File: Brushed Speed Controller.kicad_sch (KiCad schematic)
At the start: 18 parts, among them J1 Input, J2 Output, U1 TC4427, U2 TC4427, U3 SQJ500AEP-T1_GE3, U5 SQJ500AEP-T1_GE3

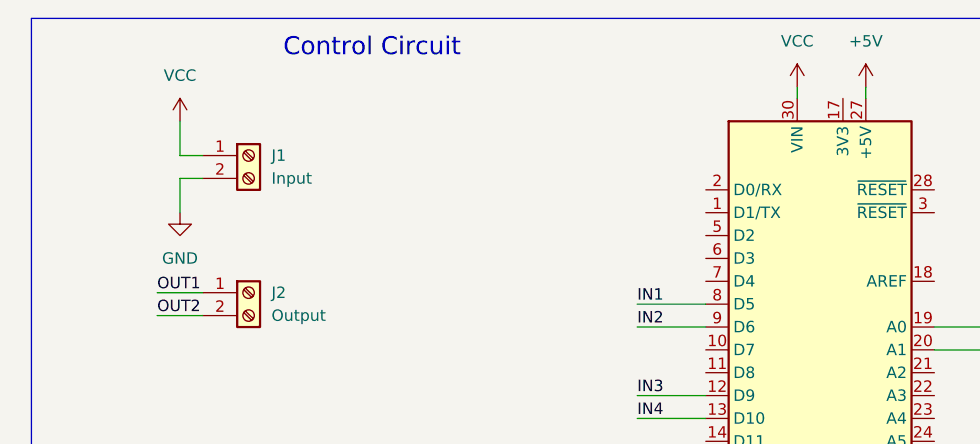
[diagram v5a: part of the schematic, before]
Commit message: Added 7805 to schematic
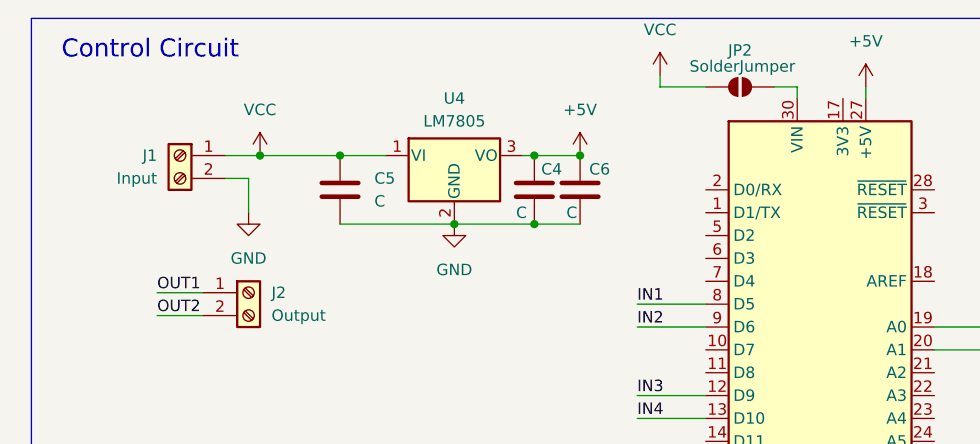
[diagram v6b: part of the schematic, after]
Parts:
- added C4, C5, C6: C, symbol Device:C
- added JP2: SolderJumper, symbol Jumper:SolderJumper_2_Open
- added U4: LM7805, Package_TO_SOT_THT:TO-220-3_Vertical, symbol Regulator_Linear:LM7805_TO220
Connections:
- net +5V: now also C4.1, C6.1, U4.3 (VO)
- net GND: now also C4.2, C5.2, C6.2, U4.2 (GND)
- net VCC: now also C5.1, JP2.1 (A), U4.1 (VI); no longer A1.30 (VIN)
- new net: A1.30 (VIN), JP2.2 (B)
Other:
- moved on the sheet: J1

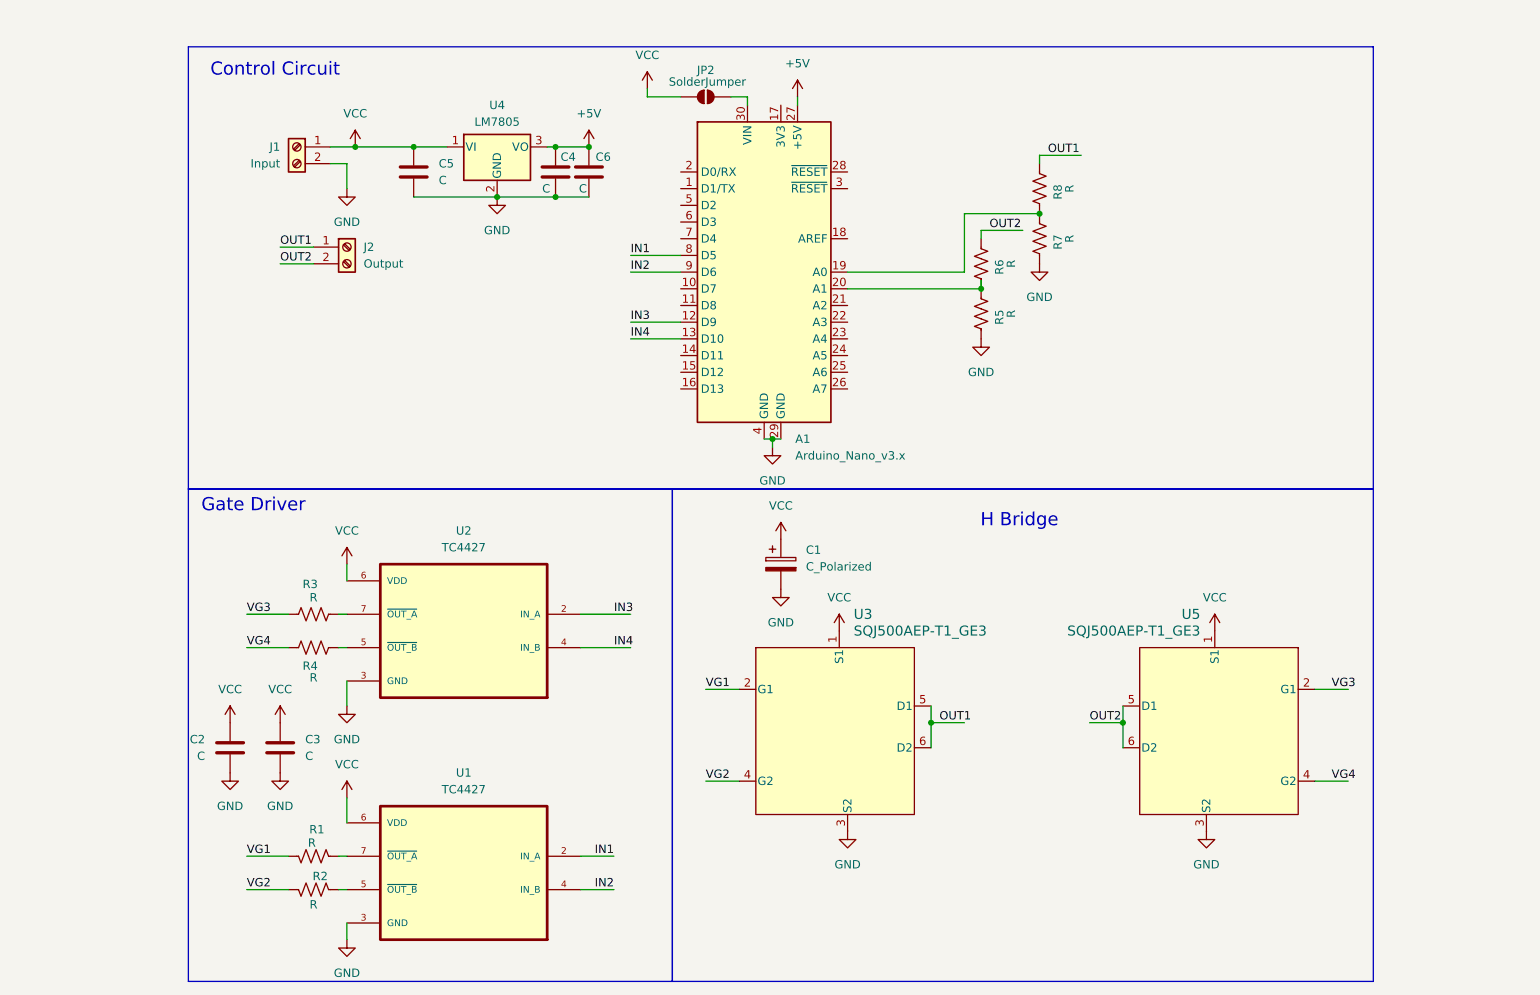
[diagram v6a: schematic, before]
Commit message: Added L7805 to PCB
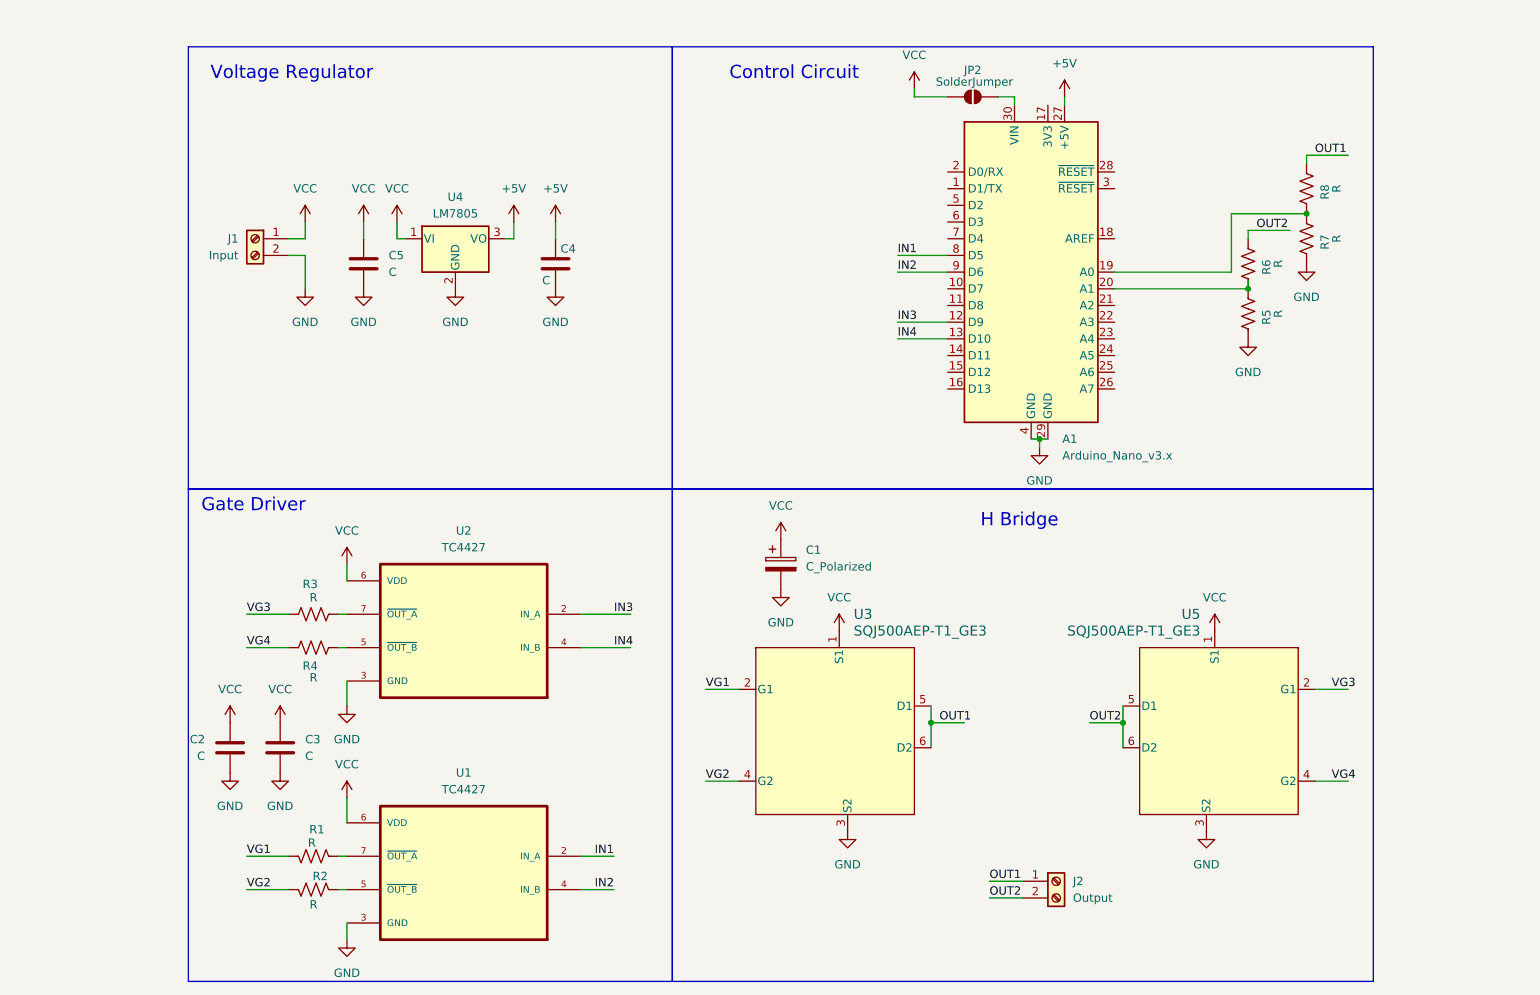
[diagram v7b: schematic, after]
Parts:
- removed C6: C, symbol Device:C
- C4, C5: footprint (none) -> Capacitor_THT:CP_Radial_D8.0mm_P5.00mm
- JP2: footprint (none) -> Jumper:SolderJumper-2_P1.3mm_Open_TrianglePad1.0x1.5mm
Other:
- note added: "Voltage Regulator"
- moved on the sheet: A1, C4, C5, J1, J2, JP2, R5, R6, R7, R8, U4

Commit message: Added bigger terminals
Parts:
- J1, J2: footprint TerminalBlock_4Ucon:TerminalBlock_4Ucon_1x02_P3.50mm_Vertical -> TerminalBlock:TerminalBlock_bornier-2_P5.08mm
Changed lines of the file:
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@@
 			)
 		)
-		(property "Footprint" "TerminalBlock_4Ucon:TerminalBlock_4Ucon_1x02_P3.50mm_Vertical"
+		(property "Footprint" "TerminalBlock:TerminalBlock_bornier-2_P5.08mm"
 			(at 184.15 148.59 0)
 			(effects
@@
 			)
 		)
-		(property "Footprint" "TerminalBlock_4Ucon:TerminalBlock_4Ucon_1x02_P3.50mm_Vertical"
+		(property "Footprint" "TerminalBlock:TerminalBlock_bornier-2_P5.08mm"
 			(at 62.23 50.8 0)
 			(effects
